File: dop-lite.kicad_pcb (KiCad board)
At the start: 2 copper layers, 50 x 50 mm, 23 parts, among them J1 Power Input, J2 Power Output, Q1 NMOS 40V×5A Vgsth<3, Q2 IRF7319, SW1 ON/OFF button, U1 IP2721_PHY, U2 LM2574N−12G_PHY

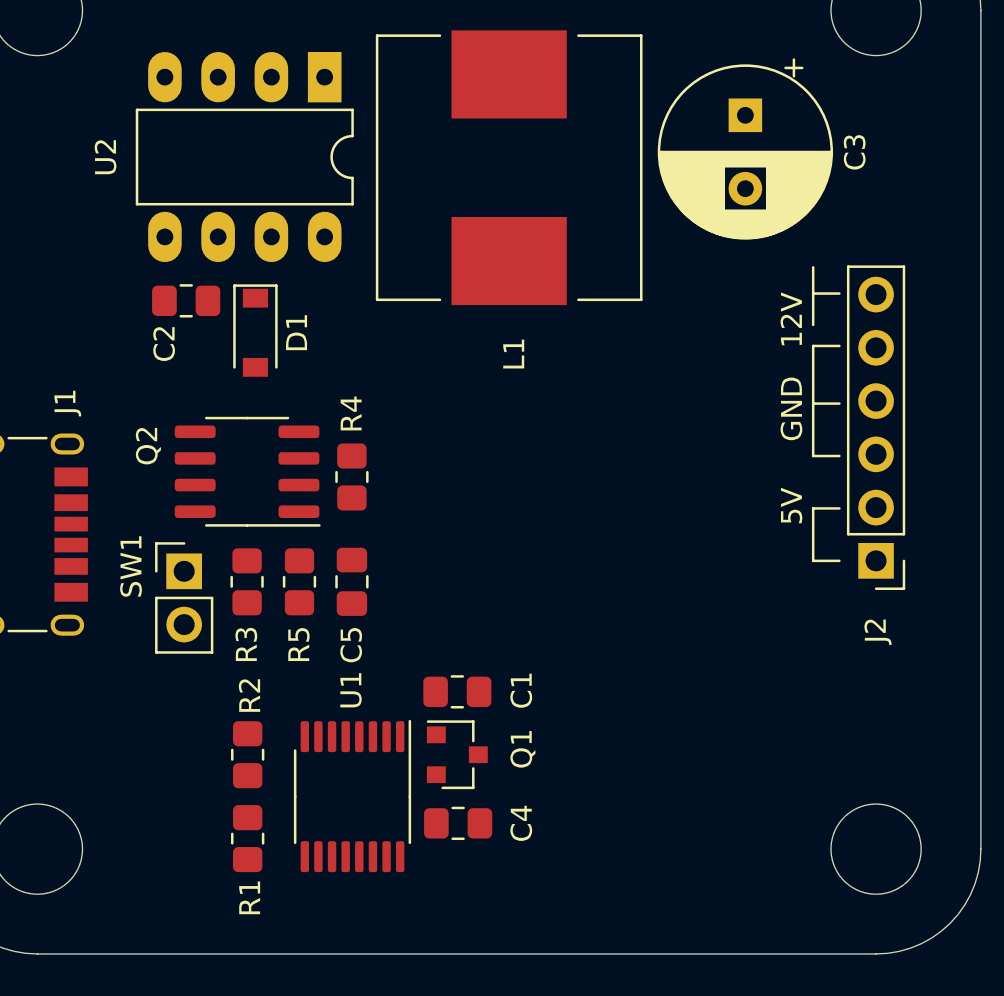
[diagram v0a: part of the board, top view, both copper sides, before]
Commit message: Renumbering of components
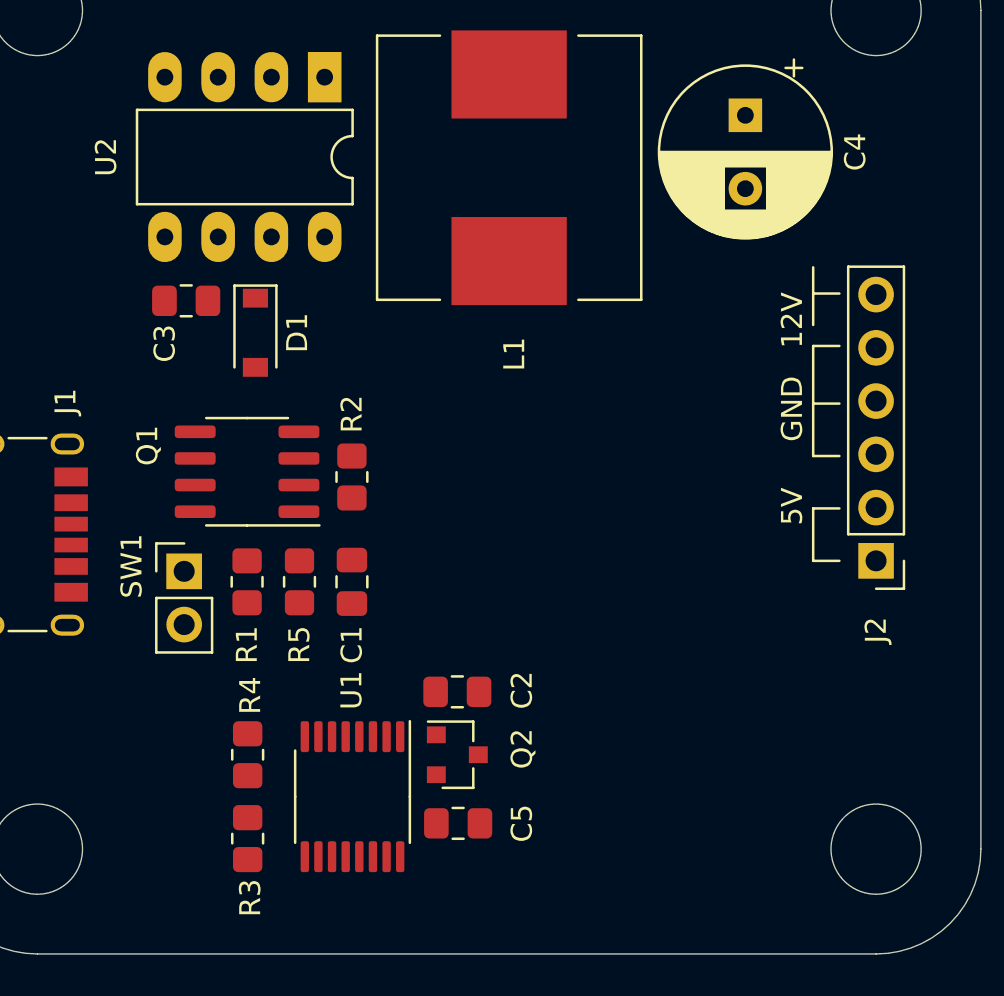
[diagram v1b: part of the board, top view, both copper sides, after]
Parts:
- renumbered C5 to C1, C1 to C2, C2 to C3, C3 to C4, C4 to C5, Q2 to Q1, Q1 to Q2, R3 to R1, R4 to R2, R1 to R3, R2 to R4
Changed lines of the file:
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@@
   (net 16 "Net-(U1-Pad4)")
   (net 17 "Net-(U1-Pad3)")
-  (net 18 "Net-(C5-Pad1)")
-  (net 19 "Net-(Q2-Pad2)")
-  (net 20 "Net-(Q2-Pad4)")
-  (net 21 /XVBUS)
-  (net 22 "Net-(R3-Pad2)")
+  (net 18 /XVBUS)
+  (net 19 "Net-(C1-Pad1)")
+  (net 20 "Net-(Q1-Pad2)")
+  (net 21 "Net-(Q1-Pad4)")
+  (net 22 "Net-(R1-Pad2)")
   (net_class Default "Ceci est la Netclass par défaut."
     (clearance 0.2)
@@
     (add_net /XVBUS)
     (add_net GND)
-    (add_net "Net-(C5-Pad1)")
+    (add_net "Net-(C1-Pad1)")
     (add_net "Net-(D1-Pad1)")
-    (add_net "Net-(Q2-Pad2)")
-    (add_net "Net-(Q2-Pad4)")
-    (add_net "Net-(R3-Pad2)")
+    (add_net "Net-(Q1-Pad2)")
+    (add_net "Net-(Q1-Pad4)")
+    (add_net "Net-(R1-Pad2)")
     (add_net "Net-(U1-Pad10)")
     (add_net "Net-(U1-Pad14)")
@@
     (fp_line (start 1.8 -1.8) (end -1.8 -1.8) (layer F.CrtYd) (width 0.05))
     (pad 2 thru_hole oval (at 0 2.54) (size 1.7 1.7) (drill 1) (layers *.Cu *.Mask)
-      (net 18 "Net-(C5-Pad1)"))
+      (net 19 "Net-(C1-Pad1)"))
     (pad 1 thru_hole rect (at 0 0) (size 1.7 1.7) (drill 1) (layers *.Cu *.Mask)
-      (net 20 "Net-(Q2-Pad4)"))
+      (net 21 "Net-(Q1-Pad4)"))
     (model ${KISYS3DMOD}/Connector_PinHeader_2.54mm.3dshapes/PinHeader_1x02_P2.54mm_Vertical.wrl
       (at (xyz 0 0 0))
@@
     (fp_line (start 1.85 0.95) (end -1.85 0.95) (layer F.CrtYd) (width 0.05))
     (pad 2 smd roundrect (at 1 0 90) (size 1.2 1.4) (layers F.Cu F.Paste F.Mask) (roundrect_rratio 0.208333)
-      (net 18 "Net-(C5-Pad1)"))
+      (net 19 "Net-(C1-Pad1)"))
     (pad 1 smd roundrect (at -1 0 90) (size 1.2 1.4) (layers F.Cu F.Paste F.Mask) (roundrect_rratio 0.208333)
-      (net 22 "Net-(R3-Pad2)"))
+      (net 22 "Net-(R1-Pad2)"))
     (model ${KISYS3DMOD}/Resistor_SMD.3dshapes/R_0805_2012Metric.wrl
       (at (xyz 0 0 0))
@@
     (tags "resistor handsolder")
     (attr smd)
-    (fp_text reference R4 (at 3 0 90) (layer F.SilkS)
+    (fp_text reference R2 (at 3 0 90) (layer F.SilkS)
       (effects (font (size 1 1) (thickness 0.15)))
     )
@@
     (fp_line (start 1.85 0.95) (end -1.85 0.95) (layer F.CrtYd) (width 0.05))
     (pad 2 smd roundrect (at 1 0 90) (size 1.2 1.4) (layers F.Cu F.Paste F.Mask) (roundrect_rratio 0.208333)
-      (net 20 "Net-(Q2-Pad4)"))
+      (net 21 "Net-(Q1-Pad4)"))
     (pad 1 smd roundrect (at -1 0 90) (size 1.2 1.4) (layers F.Cu F.Paste F.Mask) (roundrect_rratio 0.208333)
-      (net 21 /XVBUS))
+      (net 18 /XVBUS))
     (model ${KISYS3DMOD}/Resistor_SMD.3dshapes/R_0805_2012Metric.wrl
       (at (xyz 0 0 0))
@@
     (tags "resistor handsolder")
     (attr smd)
-    (fp_text reference R3 (at 3 0 90) (layer F.SilkS)
+    (fp_text reference R1 (at 3 0 90) (layer F.SilkS)
       (effects (font (size 1 1) (thickness 0.15)))
     )
@@
     (fp_line (start 1.85 0.95) (end -1.85 0.95) (layer F.CrtYd) (width 0.05))
     (pad 2 smd roundrect (at 1 0 270) (size 1.2 1.4) (layers F.Cu F.Paste F.Mask) (roundrect_rratio 0.208333)
-      (net 22 "Net-(R3-Pad2)"))
+      (net 22 "Net-(R1-Pad2)"))
     (pad 1 smd roundrect (at -1 0 270) (size 1.2 1.4) (layers F.Cu F.Paste F.Mask) (roundrect_rratio 0.208333)
       (net 2 VBUS))
@@
     (tags "SOIC SO")
     (attr smd)
-    (fp_text reference Q2 (at 4.75 1.25 270) (layer F.SilkS)
+    (fp_text reference Q1 (at 4.75 1.25 270) (layer F.SilkS)
       (effects (font (size 1 1) (thickness 0.15)))
     )
@@
       (net 2 VBUS))
     (pad 6 smd roundrect (at 2.475 0.635 180) (size 1.95 0.6) (layers F.Cu F.Paste F.Mask) (roundrect_rratio 0.25)
-      (net 19 "Net-(Q2-Pad2)"))
+      (net 20 "Net-(Q1-Pad2)"))
     (pad 5 smd roundrect (at 2.475 1.905 180) (size 1.95 0.6) (layers F.Cu F.Paste F.Mask) (roundrect_rratio 0.25)
-      (net 19 "Net-(Q2-Pad2)"))
+      (net 20 "Net-(Q1-Pad2)"))
     (pad 4 smd roundrect (at -2.475 1.905 180) (size 1.95 0.6) (layers F.Cu F.Paste F.Mask) (roundrect_rratio 0.25)
-      (net 20 "Net-(Q2-Pad4)"))
+      (net 21 "Net-(Q1-Pad4)"))
     (pad 3 smd roundrect (at -2.475 0.635 180) (size 1.95 0.6) (layers F.Cu F.Paste F.Mask) (roundrect_rratio 0.25)
       (net 1 GND))
     (pad 2 smd roundrect (at -2.475 -0.635 180) (size 1.95 0.6) (layers F.Cu F.Paste F.Mask) (roundrect_rratio 0.25)
-      (net 19 "Net-(Q2-Pad2)"))
+      (net 20 "Net-(Q1-Pad2)"))
     (pad 1 smd roundrect (at -2.475 -1.905 180) (size 1.95 0.6) (layers F.Cu F.Paste F.Mask) (roundrect_rratio 0.25)
-      (net 21 /XVBUS))
+      (net 18 /XVBUS))
     (model ${KISYS3DMOD}/Package_SO.3dshapes/SOIC-8_3.9x4.9mm_P1.27mm.wrl
       (at (xyz 0 0 0))
@@
     (tags "capacitor handsolder")
     (attr smd)
-    (fp_text reference C5 (at 3 0 90) (layer F.SilkS)
+    (fp_text reference C1 (at 3 0 90) (layer F.SilkS)
       (effects (font (size 1 1) (thickness 0.15)))
     )
@@
       (net 1 GND))
     (pad 1 smd roundrect (at -1.0375 0 270) (size 1.175 1.45) (layers F.Cu F.Paste F.Mask) (roundrect_rratio 0.212766)
-      (net 18 "Net-(C5-Pad1)"))
+      (net 19 "Net-(C1-Pad1)"))
     (model ${KISYS3DMOD}/Capacitor_SMD.3dshapes/C_0805_2012Metric.wrl
       (at (xyz 0 0 0))
@@
       (net 17 "Net-(U1-Pad3)"))
     (pad 2 smd roundrect (at -2.8625 -1.625 270) (size 1.475 0.4) (layers F.Cu F.Paste F.Mask) (roundrect_rratio 0.25)
-      (net 21 /XVBUS))
+      (net 18 /XVBUS))
     (pad 1 smd roundrect (at -2.8625 -2.275 270) (size 1.475 0.4) (layers F.Cu F.Paste F.Mask) (roundrect_rratio 0.25)
       (net 8 /GATE))
@@
     (tags "resistor handsolder")
     (attr smd)
-    (fp_text reference R2 (at 2.82362 0.13194 90) (layer F.SilkS)
+    (fp_text reference R4 (at 2.82362 0.13194 90) (layer F.SilkS)
       (effects (font (size 1 1) (thickness 0.15)))
     )
@@
     (tags "resistor handsolder")
     (attr smd)
-    (fp_text reference R1 (at 2.82838 -0.13194 90) (layer F.SilkS)
+    (fp_text reference R3 (at 2.82838 -0.13194 90) (layer F.SilkS)
       (effects (font (size 1 1) (thickness 0.15)))
     )
@@
     (tags SOT-23)
     (attr smd)
-    (fp_text reference Q1 (at 3.08594 -0.28362 90) (layer F.SilkS)
+    (fp_text reference Q2 (at 3.08594 -0.28362 90) (layer F.SilkS)
       (effects (font (size 1 1) (thickness 0.15)))
     )
@@
     (tags "capacitor handsolder")
     (attr smd)
-    (fp_text reference C4 (at 3.048 0 90) (layer F.SilkS)
+    (fp_text reference C5 (at 3.048 0 90) (layer F.SilkS)
       (effects (font (size 1 1) (thickness 0.15)))
     )
@@
     (descr "CP, Radial series, Radial, pin pitch=3.50mm, , diameter=8mm, Electrolytic Capacitor")
     (tags "CP Radial series Radial pin pitch 3.50mm  diameter 8mm Electrolytic Capacitor")
-    (fp_text reference C3 (at 1.75 -5.25 90) (layer F.SilkS)
+    (fp_text reference C4 (at 1.75 -5.25 90) (layer F.SilkS)
       (effects (font (size 1 1) (thickness 0.15)))
     )
@@
     (tags "capacitor handsolder")
     (attr smd)
-    (fp_text reference C2 (at -1.016 2.032 90) (layer F.SilkS)
+    (fp_text reference C3 (at -1.016 2.032 90) (layer F.SilkS)
       (effects (font (size 1 1) (thickness 0.15)))
     )
@@
     (tags "capacitor handsolder")
     (attr smd)
-    (fp_text reference C1 (at -3.08594 0.07762 90) (layer F.SilkS)
-      (effects (font (size 1 1) (thickness 0.15)))
-    )
+    (fp_text reference C2 (at -3.08594 0.07762 90) (layer F.SilkS)
+      (effects (font (size 1 1) (thickness 0.15)))
+    )

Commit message: Conception rules
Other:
- copper layers 2 -> 4
- net class 1 Amp added: clearance 0.2, trace_width 0.2, via_dia 0.4, via_drill 0.2
- net class 2 Amp added: clearance 0.2, trace_width 0.8, via_dia 0.5, via_drill 0.3
- net class 3 Amp added: clearance 0.2, trace_width 1.4, via_dia 0.7, via_drill 0.5
- net class 4 Amp added: clearance 0.2, trace_width 2.1, via_dia 0.9, via_drill 0.7
- net class Default: trace_width 0.25 -> 0.2; via_dia 0.8 -> 0.4; via_drill 0.4 -> 0.2
- rule via_min_drill: 0.3 -> 0.2
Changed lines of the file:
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@@
   (layers
     (0 F.Cu signal)
+    (1 In1.Cu power)
+    (2 In2.Cu power)
     (31 B.Cu signal)
     (32 B.Adhes user)
@@
   )
   (setup
-    (last_trace_width 0.25)
+    (last_trace_width 0.2)
+    (user_trace_width 0.2)
+    (user_trace_width 0.8)
+    (user_trace_width 1.4)
+    (user_trace_width 2.1)
     (trace_clearance 0.2)
     (zone_clearance 0.508)
     (zone_45_only no)
     (trace_min 0.2)
-    (via_size 0.8)
-    (via_drill 0.4)
+    (via_size 0.4)
+    (via_drill 0.2)
     (via_min_size 0.4)
-    (via_min_drill 0.3)
+    (via_min_drill 0.2)
+    (user_via 0.4 0.2)
+    (user_via 0.5 0.3)
+    (user_via 0.7 0.5)
+    (user_via 0.9 0.7)
     (uvia_size 0.3)
     (uvia_drill 0.1)
@@
   (net_class Default "Ceci est la Netclass par défaut."
     (clearance 0.2)
-    (trace_width 0.25)
-    (via_dia 0.8)
-    (via_drill 0.4)
+    (trace_width 0.2)
+    (via_dia 0.4)
+    (via_drill 0.2)
     (uvia_dia 0.3)
     (uvia_drill 0.1)
@@
     (add_net VBUS)
   )
+  (net_class "1 Amp" ""
+    (clearance 0.2)
+    (trace_width 0.2)
+    (via_dia 0.4)
+    (via_drill 0.2)
+    (uvia_dia 0.3)
+    (uvia_drill 0.1)
+  )
+  (net_class "2 Amp" ""
+    (clearance 0.2)
+    (trace_width 0.8)
+    (via_dia 0.5)
+    (via_drill 0.3)
+    (uvia_dia 0.3)
+    (uvia_drill 0.1)
+  )
+  (net_class "3 Amp" ""
+    (clearance 0.2)
+    (trace_width 1.4)
+    (via_dia 0.7)
+    (via_drill 0.5)
+    (uvia_dia 0.3)
+    (uvia_drill 0.1)
+  )
+  (net_class "4 Amp" ""
+    (clearance 0.2)
+    (trace_width 2.1)
+    (via_dia 0.9)
+    (via_drill 0.7)
+    (uvia_dia 0.3)
+    (uvia_drill 0.1)
+  )
   (module Connector_PinHeader_2.54mm:PinHeader_1x02_P2.54mm_Vertical (layer F.Cu)

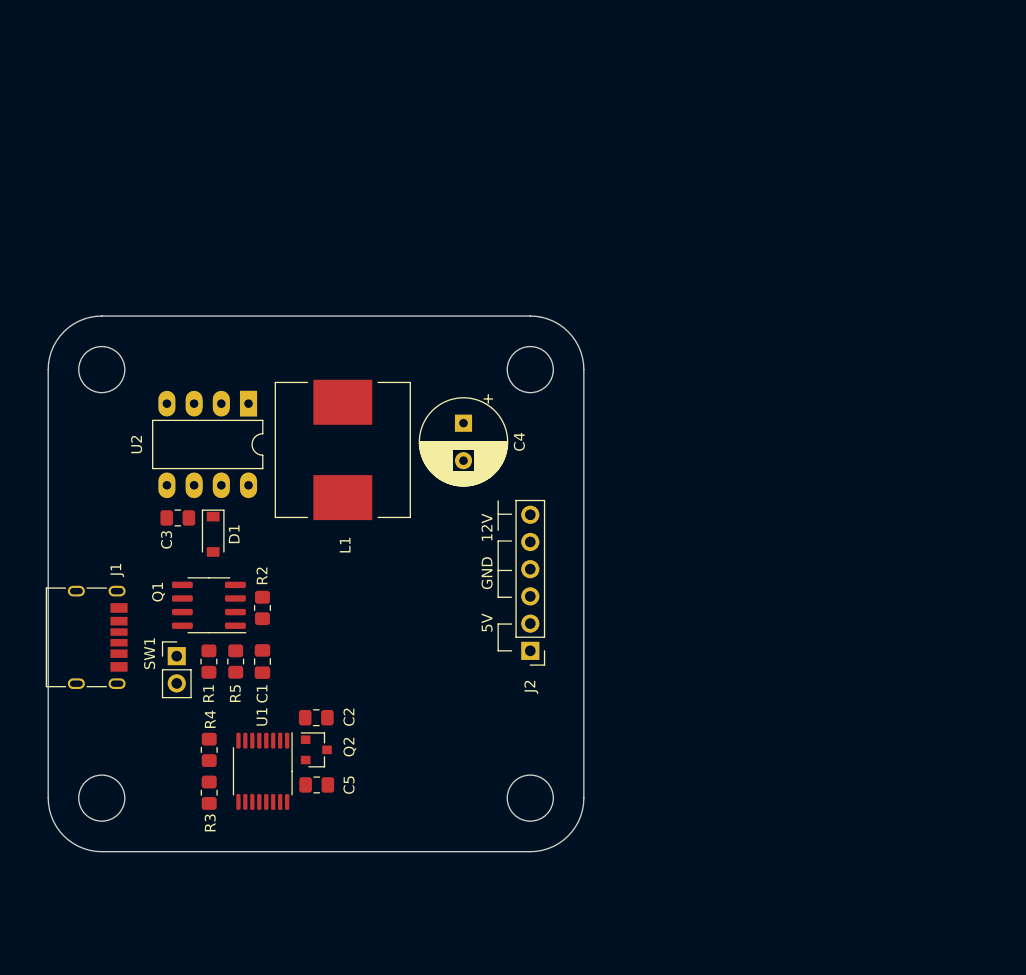
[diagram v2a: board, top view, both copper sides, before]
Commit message: fixed wrong use of vbus vs xvbus, finished pcb draft
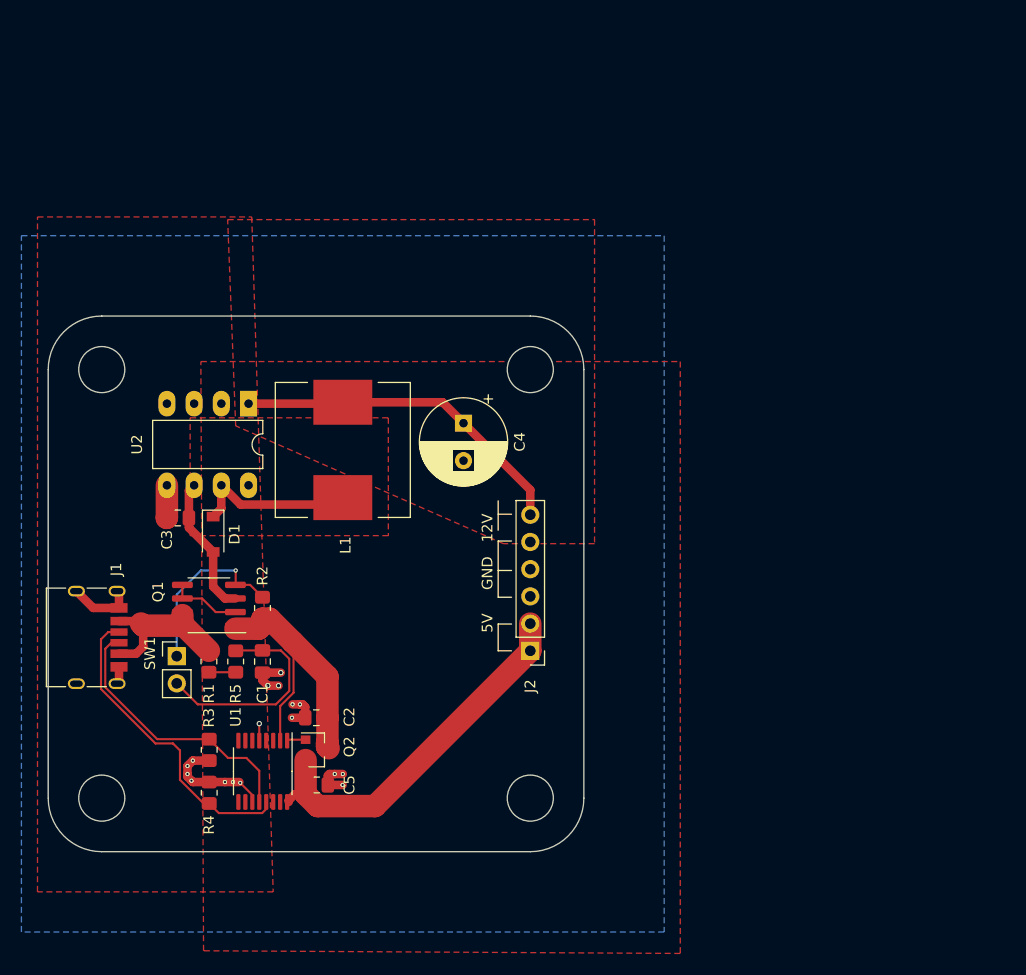
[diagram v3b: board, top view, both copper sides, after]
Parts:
- moved R4 4.00 mm to (65.0, 169.5)
- moved R3 4.00 mm to (65.0, 165.5)
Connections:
- C2 pad 1: VBUS -> /XVBUS
- Q2 pad 3: VBUS -> /XVBUS
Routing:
- net GND: track 0.00 -> 45.0 mm, vias 0 -> 17
- net /5V_OUT: track 0.00 -> 38.2 mm
- net /12V_OUT: track 0.00 -> 32.1 mm
- net /CC1: track 0.00 -> 29.9 mm
- net /XVBUS: track 0.00 -> 28.1 mm
- net /CC2: track 0.00 -> 25.6 mm
- net Net-(C1-Pad1): track 0.00 -> 20.2 mm
- net Net-(Q1-Pad4): track 0.00 -> 16.5 mm, vias 0 -> 1
- net Net-(D1-Pad1): track 0.00 -> 15.6 mm
- net VBUS: track 0.00 -> 15.3 mm
- net Net-(Q1-Pad2): track 0.00 -> 6.75 mm
- net Net-(R1-Pad2): track 0.00 -> 2.50 mm
- net /GATE: track 0.00 -> 1.76 mm
- added copper zone on F.Cu, net /12V_OUT
- added copper zone on B.Cu, net /5V_OUT
- added copper zone on F.Cu, net /5V_OUT
- added copper zone on In1.Cu, net GND
- added copper zone on In2.Cu, net GND
- added copper zone on F.Cu, net Net-(D1-Pad1)
- added copper zone on F.Cu, net VBUS

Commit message: decorate PCB (cc-0 logos, disclaimer, title)
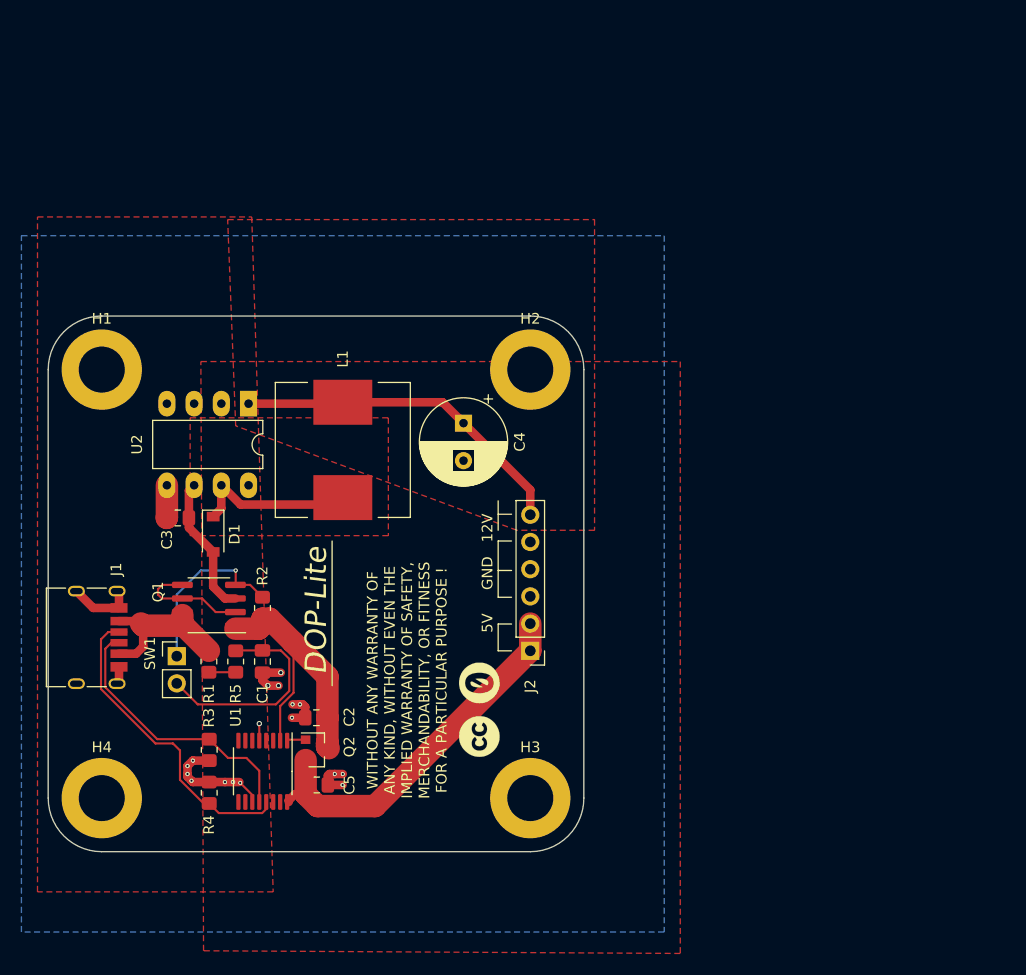
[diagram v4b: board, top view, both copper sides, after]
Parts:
- added G***: LOGO, cliparts:logo--cc--zero, F.Cu at (90.2, 159.2)
- added G***: LOGO, cliparts:logo--cc--cc, F.Cu at (90.2, 164.2)
- H1, H2, H3, H4: footprint MountingHole:MountingHole_4.3mm_M4 -> MountingHole:MountingHole_4.3mm_M4_DIN965_Pad
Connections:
- net GND renamed /GND
- net VBUS renamed Net-(J1-PadA9)
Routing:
- net Net-(Q1-Pad2): track 6.75 -> 10.8 mm
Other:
- board text added: "DOP-Lite"
- board text added: "WITHOUT ANY WARRANTY OF ANY KIND, WITHOUT EVEN THE IMPLIED WARRANTY OF SAFETY, MERCHANDABILITY, OR FITNESS FOR A PARTICULAR PURPOSE !"
